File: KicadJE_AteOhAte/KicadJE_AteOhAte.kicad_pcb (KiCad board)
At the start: 2 copper layers, 100 x 100 mm, 201 parts, among them J201 In_Accent, J202 In Gate, J203 Out Tom, J301 PJRAS2X2S01AUX, J302 Conn_01x03, P201 Doepfer_Power_10pin, Q201 MMBT2222A, Q202 MMBT2222A, Q203 MMBT2222A, Q204 MMBT2222A, Q205 MMBT2907A, Q206 MMBT2222A, Q207 MMBT2222A, SW201 Con/Tom, U201 TL072, U202 TL072, U203 TL072, U301 TL072, U302 TL072, U303 TL072

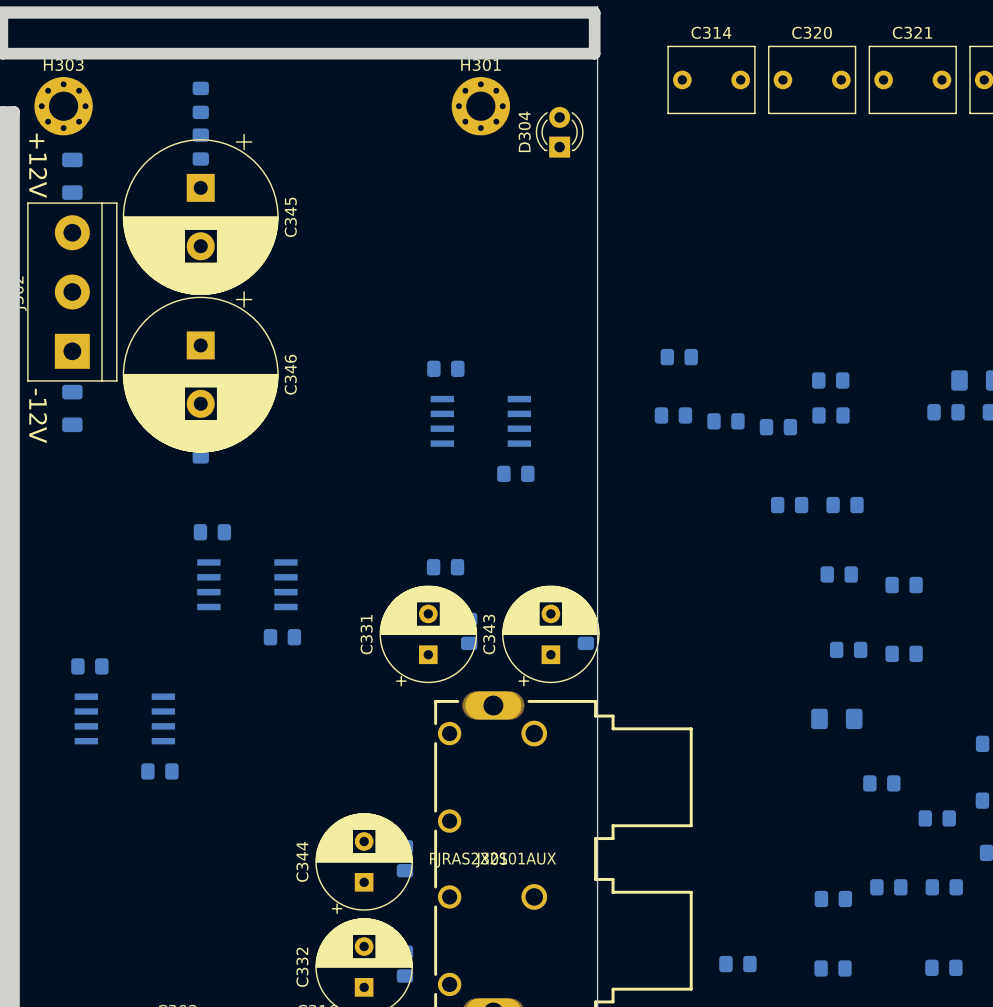
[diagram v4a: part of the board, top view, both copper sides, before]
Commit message: SCH Error in RIAA fixed (link C313 327 area)
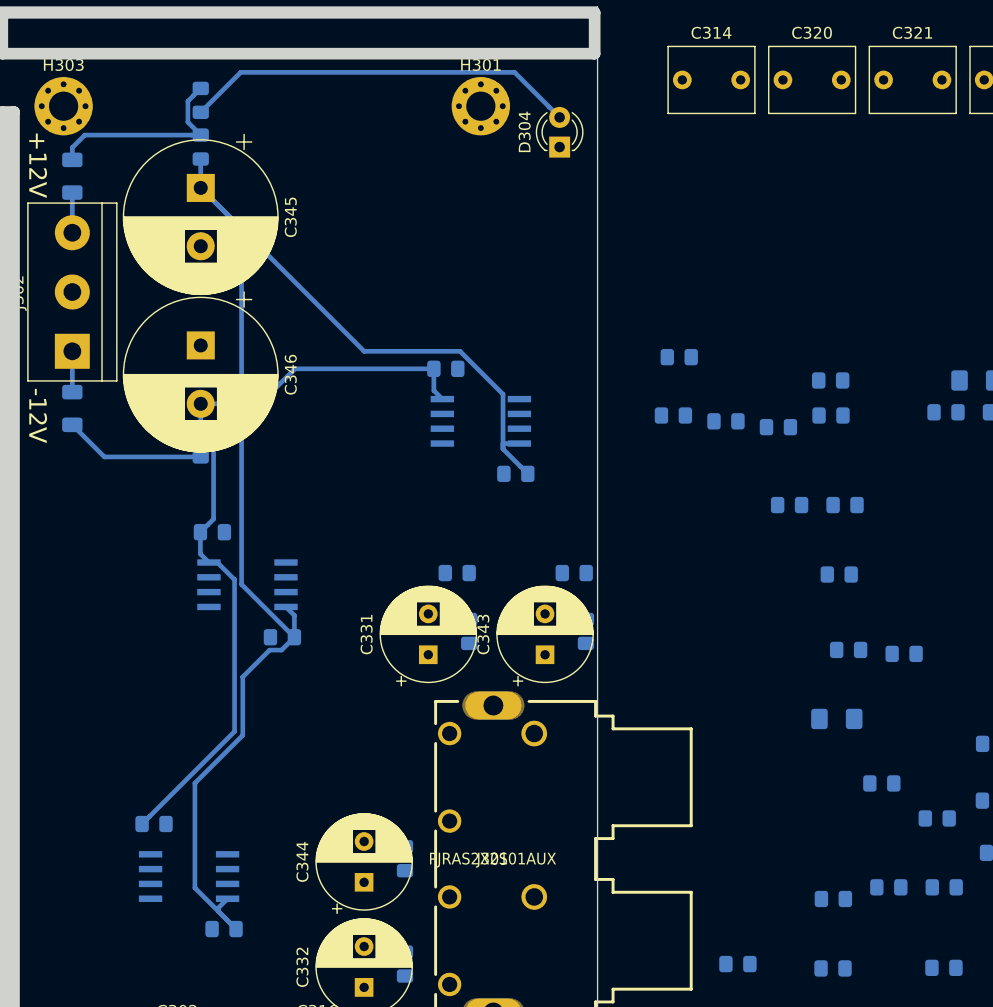
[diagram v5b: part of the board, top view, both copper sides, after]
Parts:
- moved R328 28.3 mm to (148.0, 98.5)
- moved C336 14.6 mm to (118.0, 129.0)
- moved C338 14.6 mm to (112.0, 120.0)
- moved U303 14.6 mm to (115.0, 124.5)
- moved R326 1.12 mm to (138.0, 98.5)
- moved C343 0.50 mm to (145.5, 105.5)
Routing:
- net +12V: track 238.2 -> 362.3 mm
- net -12V: track 154.8 -> 220.8 mm, vias 0 -> 2
- net Net-(D304-Pad2): track 0.00 -> 33.8 mm
- net Net-(F301-Pad2): track 0.00 -> 17.4 mm
- net Net-(D304-Pad1): track 0.00 -> 12.1 mm
- net /KicadJE_AteOhAte3/-PSU: track 0.00 -> 3.50 mm
- net /KicadJE_AteOhAte3/+PSU: track 0.00 -> 3.44 mm
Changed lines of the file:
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@@
     (thickness 1.6)
     (drawings 42)
-    (tracks 776)
+    (tracks 837)
     (zones 0)
     (modules 201)
@@
     (add_net /KicadJE_AteOhAte2/PinkNoise)
     (add_net /KicadJE_AteOhAte2/WhiteNoise)
-    (add_net /KicadJE_AteOhAte3/+PSU)
-    (add_net /KicadJE_AteOhAte3/-PSU)
     (add_net InAccent)
     (add_net InGate)
@@
     (add_net "Net-(D205-Pad1)")
     (add_net "Net-(D208-Pad2)")
-    (add_net "Net-(D304-Pad1)")
-    (add_net "Net-(D304-Pad2)")
-    (add_net "Net-(F301-Pad2)")
     (add_net "Net-(J201-PadT)")
     (add_net "Net-(J202-PadT)")
@@
     (add_net +12V)
     (add_net -12V)
+    (add_net /KicadJE_AteOhAte3/+PSU)
+    (add_net /KicadJE_AteOhAte3/-PSU)
     (add_net GND)
+    (add_net "Net-(D304-Pad1)")
+    (add_net "Net-(D304-Pad2)")
+    (add_net "Net-(F301-Pad2)")
   )
   (module AJ:Johansen_engineering_logo_25mm_front_neg5 (layer B.Cu)
@@
   )
   (module Capacitor_SMD:C_0805_2012Metric_Pad1.15x1.40mm_HandSolder (layer B.Cu)
-    (at 112.5 115.5)
+    (at 118 129)
     (descr "Capacitor SMD 0805 (2012 Metric), square (rectangular) end terminal, IPC_7351 nominal with elongated pad for handsoldering. (Body size source: https://docs.google.com/spreadsheets/d/1BsfQQcO9C6DZCsRaXUlFlo91Tg2WpOkGARC1WS5S8t0/edit?usp=sharing), generated with kicad-footprint-generator")
     (tags "capacitor handsolder")
@@
   )
   (module Capacitor_SMD:C_0805_2012Metric_Pad1.15x1.40mm_HandSolder (layer B.Cu)
-    (at 106.5 106.5)
+    (at 112 120)
     (descr "Capacitor SMD 0805 (2012 Metric), square (rectangular) end terminal, IPC_7351 nominal with elongated pad for handsoldering. (Body size source: https://docs.google.com/spreadsheets/d/1BsfQQcO9C6DZCsRaXUlFlo91Tg2WpOkGARC1WS5S8t0/edit?usp=sharing), generated with kicad-footprint-generator")
     (tags "capacitor handsolder")
@@
   )
   (module Resistor_SMD:R_0805_2012Metric_Pad1.15x1.40mm_HandSolder (layer B.Cu)
-    (at 136.975 98)
+    (at 137.975 98.5)
     (descr "Resistor SMD 0805 (2012 Metric), square (rectangular) end terminal, IPC_7351 nominal with elongated pad for handsoldering. (Body size source: https://docs.google.com/spreadsheets/d/1BsfQQcO9C6DZCsRaXUlFlo91Tg2WpOkGARC1WS5S8t0/edit?usp=sharing), generated with kicad-footprint-generator")
     (tags "resistor handsolder")
@@
   )
   (module Resistor_SMD:R_0805_2012Metric_Pad1.15x1.40mm_HandSolder (layer B.Cu)
-    (at 176.265001 99.524999)
+    (at 148 98.5)
     (descr "Resistor SMD 0805 (2012 Metric), square (rectangular) end terminal, IPC_7351 nominal with elongated pad for handsoldering. (Body size source: https://docs.google.com/spreadsheets/d/1BsfQQcO9C6DZCsRaXUlFlo91Tg2WpOkGARC1WS5S8t0/edit?usp=sharing), generated with kicad-footprint-generator")
     (tags "resistor handsolder")
@@
   )
   (module AJ-Dropbox-Kicad:AJ_SO-8_5.3x6.2mm_P1.27mm (layer B.Cu)
-    (at 109.5 111)
+    (at 115 124.5)
     (descr "8-Lead Plastic Small Outline, 5.3x6.2mm Body (http://www.ti.com.cn/cn/lit/ds/symlink/tl7705a.pdf)")
     (tags "SOIC 1.27")
@@
   )
   (module Capacitor_THT:CP_Radial_D8.0mm_P3.50mm (layer F.Cu)
-    (at 146 105.5 90)
+    (at 145.5 105.5 90)
     (descr "CP, Radial series, Radial, pin pitch=3.50mm, , diameter=8mm, Electrolytic Capacitor")
     (tags "CP Radial series Radial pin pitch 3.50mm  diameter 8mm Electrolytic Capacitor")
@@
   (segment (start 74.39996 122.60004) (end 72.475 124.525) (width 0.4) (layer B.Cu) (net 3))
   (segment (start 94 66) (end 91.46 66) (width 0.4) (layer F.Cu) (net 3) (status 30))
+  (segment (start 116 84) (end 116 86.5) (width 0.4) (layer B.Cu) (net 3))
+  (segment (start 116.598372 94.376628) (end 115.975 95) (width 0.4) (layer B.Cu) (net 3))
+  (segment (start 117.10001 93.87499) (end 116.598372 94.376628) (width 0.4) (layer B.Cu) (net 3))
+  (segment (start 117.10001 87.60001) (end 117.10001 93.87499) (width 0.4) (layer B.Cu) (net 3))
+  (segment (start 116 86.5) (end 117.10001 87.60001) (width 0.4) (layer B.Cu) (net 3))
+  (segment (start 115.975 96.87) (end 116.7 97.595) (width 0.4) (layer B.Cu) (net 3))
+  (segment (start 115.975 95) (end 115.975 96.87) (width 0.4) (layer B.Cu) (net 3))
+  (via (at 118.69999 84) (size 0.8) (drill 0.4) (layers F.Cu B.Cu) (net 3))
+  (segment (start 118.899989 112.075011) (end 111.598372 119.376628) (width 0.4) (layer B.Cu) (net 3))
+  (segment (start 111.598372 119.376628) (end 110.975 120) (width 0.4) (layer B.Cu) (net 3))
+  (segment (start 118.899989 99.069989) (end 118.899989 112.075011) (width 0.4) (layer B.Cu) (net 3))
+  (segment (start 117.425 97.595) (end 118.899989 99.069989) (width 0.4) (layer B.Cu) (net 3))
+  (segment (start 116.7 97.595) (end 117.425 97.595) (width 0.4) (layer B.Cu) (net 3))
+  (segment (start 116 84) (end 118.69999 84) (width 0.4) (layer B.Cu) (net 3))
+  (via (at 120.5 84) (size 0.8) (drill 0.4) (layers F.Cu B.Cu) (net 3))
+  (segment (start 118.69999 84) (end 120.5 84) (width 0.4) (layer F.Cu) (net 3))
+  (segment (start 121.065685 84) (end 120.5 84) (width 0.4) (layer B.Cu) (net 3))
+  (segment (start 135.975 81) (end 124.065685 81) (width 0.4) (layer B.Cu) (net 3))
+  (segment (start 124.065685 81) (end 121.065685 84) (width 0.4) (layer B.Cu) (net 3))
+  (segment (start 135.975 82.87) (end 136.7 83.595) (width 0.4) (layer B.Cu) (net 3))
+  (segment (start 135.975 81) (end 135.975 82.87) (width 0.4) (layer B.Cu) (net 3))
   (segment (start 81 126.8) (end 81 128.475) (width 0.4) (layer B.Cu) (net 4) (status 30))
   (segment (start 80.93 128.405) (end 81 128.475) (width 0.4) (layer B.Cu) (net 4) (status 30))
@@
   (segment (start 70.905 64.7) (end 70.905 67.905) (width 0.4) (layer B.Cu) (net 4) (status 10))
   (segment (start 70.905 67.905) (end 73 70) (width 0.4) (layer B.Cu) (net 4))
+  (segment (start 116 63.025) (end 116 65.5) (width 0.4) (layer B.Cu) (net 4))
+  (segment (start 124.025 102.13) (end 123.3 101.405) (width 0.4) (layer B.Cu) (net 4))
+  (segment (start 124.025 104) (end 124.025 102.13) (width 0.4) (layer B.Cu) (net 4))
+  (segment (start 143.401628 89.376628) (end 144.025 90) (width 0.4) (layer B.Cu) (net 4))
+  (segment (start 141.899999 87.874999) (end 143.401628 89.376628) (width 0.4) (layer B.Cu) (net 4))
+  (segment (start 141.899999 83.180743) (end 141.899999 87.874999) (width 0.4) (layer B.Cu) (net 4))
+  (segment (start 138.219256 79.5) (end 141.899999 83.180743) (width 0.4) (layer B.Cu) (net 4))
+  (segment (start 116 65.5) (end 130 79.5) (width 0.4) (layer B.Cu) (net 4))
+  (segment (start 130 79.5) (end 138.219256 79.5) (width 0.4) (layer B.Cu) (net 4))
+  (segment (start 117.5 127.205) (end 118.3 126.405) (width 0.4) (layer B.Cu) (net 4))
+  (segment (start 119.025 129) (end 117.5 127.475) (width 0.4) (layer B.Cu) (net 4))
+  (segment (start 117.5 127.475) (end 117.5 127.205) (width 0.4) (layer B.Cu) (net 4))
+  (segment (start 115.5 125.475) (end 119.025 129) (width 0.4) (layer B.Cu) (net 4))
+  (segment (start 122.92499 105.10001) (end 121.89999 105.10001) (width 0.4) (layer B.Cu) (net 4))
+  (segment (start 124.025 104) (end 122.92499 105.10001) (width 0.4) (layer B.Cu) (net 4))
+  (segment (start 121.89999 105.10001) (end 119.60001 107.39999) (width 0.4) (layer B.Cu) (net 4))
+  (segment (start 119.60001 107.39999) (end 119.60001 112.39999) (width 0.4) (layer B.Cu) (net 4))
+  (segment (start 119.60001 112.39999) (end 115.5 116.5) (width 0.4) (layer B.Cu) (net 4))
+  (segment (start 115.5 116.5) (end 115.5 125.475) (width 0.4) (layer B.Cu) (net 4))
+  (segment (start 116 65.5) (end 119.5 69) (width 0.4) (layer B.Cu) (net 4))
+  (segment (start 119.5 69) (end 119.5 99.475) (width 0.4) (layer B.Cu) (net 4))
+  (segment (start 119.5 99.475) (end 124.025 104) (width 0.4) (layer B.Cu) (net 4))
+  (segment (start 141.9 87.405) (end 143.3 87.405) (width 0.4) (layer B.Cu) (net 4))
+  (segment (start 141.899999 87.874999) (end 141.9 87.405) (width 0.4) (layer B.Cu) (net 4))
   (segment (start 65.549999 142.7) (end 65.575 142.674999) (width 0.15) (layer B.Cu) (net 9) (status 30))
   (segment (start 63.875 142.7) (end 65.549999 142.7) (width 0.15) (layer B.Cu) (net 9) (status 30))
@@
   (segment (start 73.774989 126.5) (end 72.485 126.5) (width 0.15) (layer B.Cu) (net 65))
   (segment (start 72.485 126.5) (end 71.85 127.135) (width 0.15) (layer B.Cu) (net 65))
+  (segment (start 145.850001 58.560001) (end 146.75 59.46) (width 0.4) (layer B.Cu) (net 90))
+  (segment (start 142.889999 55.599999) (end 145.850001 58.560001) (width 0.4) (layer B.Cu) (net 90))
+  (segment (start 119.425001 55.599999) (end 142.889999 55.599999) (width 0.4) (layer B.Cu) (net 90))
+  (segment (start 116 59.025) (end 119.425001 55.599999) (width 0.4) (layer B.Cu) (net 90))
+  (segment (start 107.75 88.55) (end 105 85.8) (width 0.4) (layer B.Cu) (net 91))
+  (segment (start 116 88.55) (end 107.75 88.55) (width 0.4) (layer B.Cu) (net 91))
+  (segment (start 105 79.5) (end 105 83) (width 0.4) (layer B.Cu) (net 100))
+  (segment (start 105 69.34) (end 105 65.9) (width 0.4) (layer B.Cu) (net 101))
+  (segment (start 115.2 60.975) (end 116 60.975) (width 0.4) (layer B.Cu) (net 102))
+  (segment (start 106.067002 60.975) (end 115.2 60.975) (width 0.4) (layer B.Cu) (net 102))
+  (segment (start 105 62.042002) (end 106.067002 60.975) (width 0.4) (layer B.Cu) (net 102))
+  (segment (start 105 63.1) (end 105 62.042002) (width 0.4) (layer B.Cu) (net 102))
+  (segment (start 115.376628 57.598372) (end 116 56.975) (width 0.4) (layer B.Cu) (net 102))
+  (segment (start 114.89999 58.07501) (end 115.376628 57.598372) (width 0.4) (layer B.Cu) (net 102))
+  (segment (start 114.89999 59.87499) (end 114.89999 58.07501) (width 0.4) (layer B.Cu) (net 102))
+  (segment (start 116 60.975) (end 114.89999 59.87499) (width 0.4) (layer B.Cu) (net 102))
   (zone (net 1) (net_name GND) (layer B.Cu) (hatch edge 0.508)
     (connect_pads (clearance 0.508))

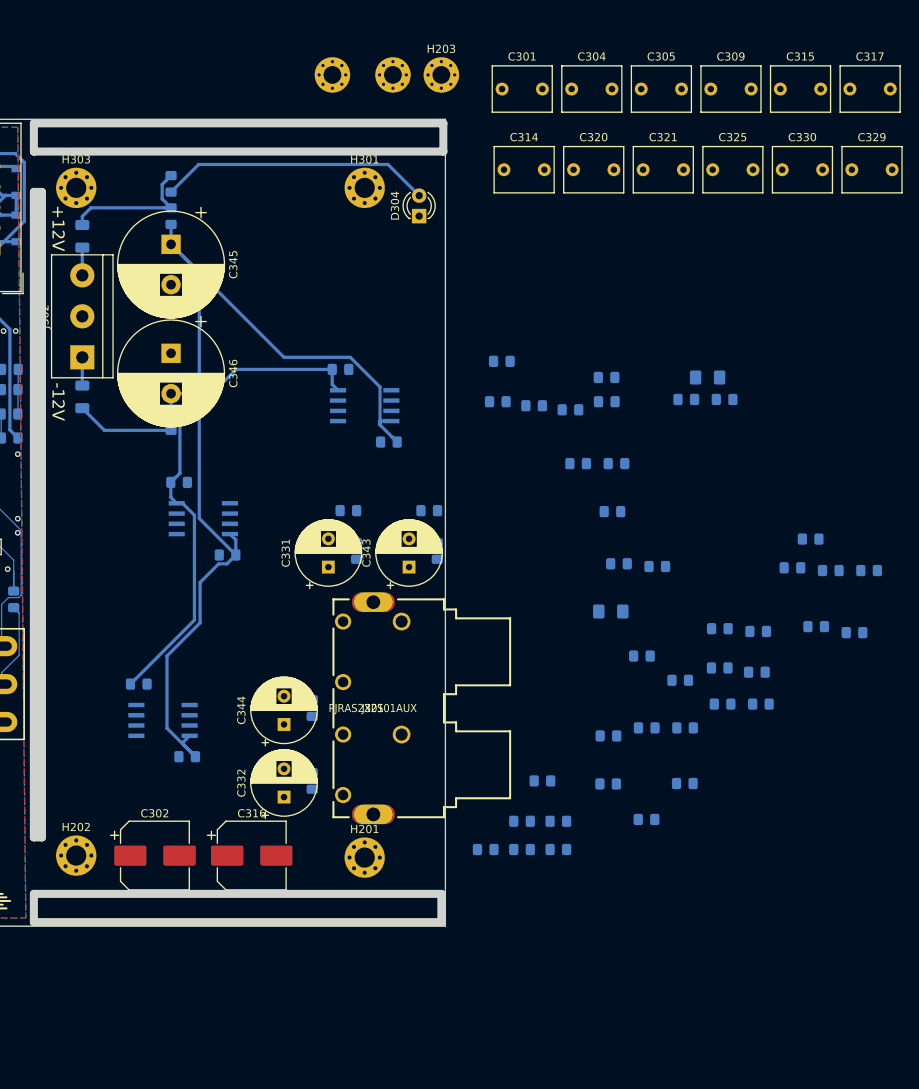
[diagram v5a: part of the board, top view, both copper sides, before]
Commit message: 90% component placement RIAA
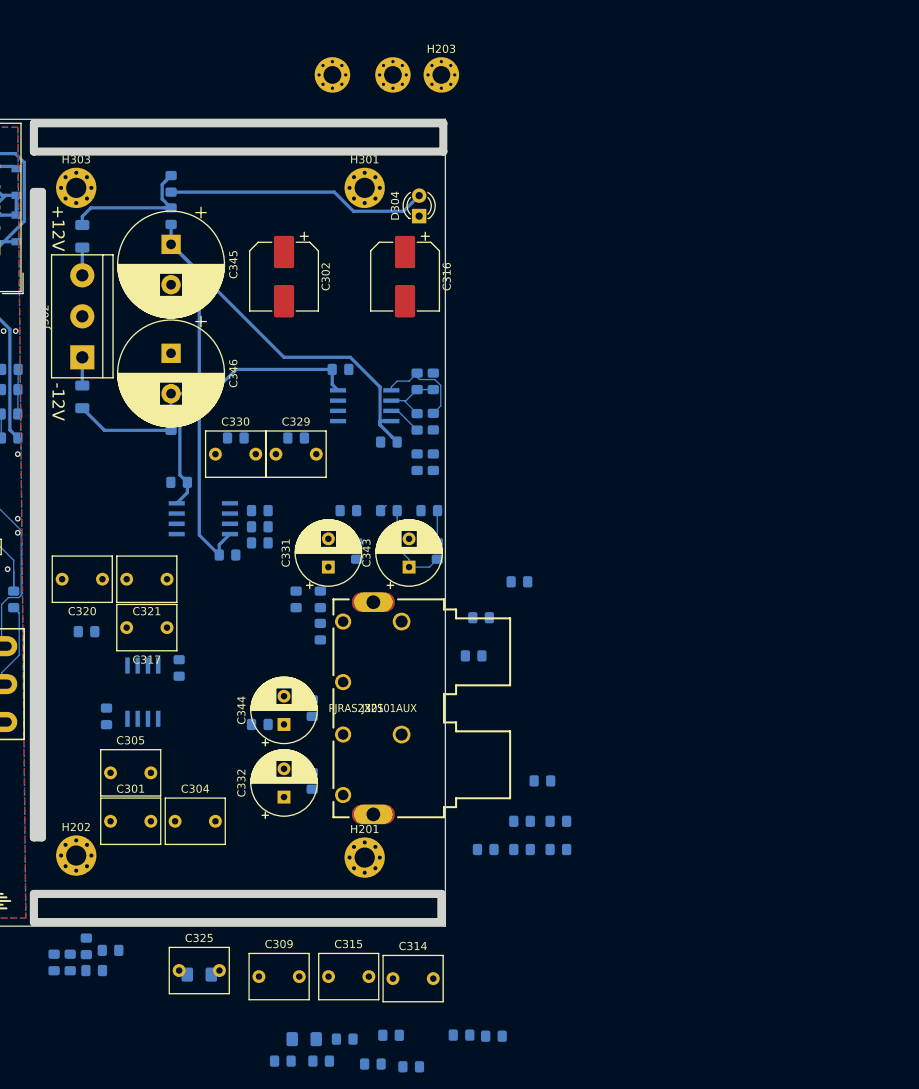
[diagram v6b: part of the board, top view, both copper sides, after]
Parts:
- moved C309 123.4 mm to (126.9, 156.2)
- moved C315 123.4 mm to (135.5, 156.2)
- moved C325 119.3 mm to (117.0, 155.5)
- moved C317 107.8 mm to (115.5, 113.0), turned to 180 degrees
- moved C305 107.3 mm to (108.5, 131.0)
- moved C304 103.2 mm to (116.5, 137.0)
- moved C301 102.9 mm to (108.5, 137.0)
- moved C314 101.2 mm to (143.5, 156.5)
- moved R323 99.1 mm to (106.5, 155.5), turned to 180 degrees
- moved C311 96.0 mm to (132.5, 164.0)
- moved R308 96.0 mm to (129.9, 166.7)
- moved R312 96.0 mm to (134.6, 166.7)
- moved R316 95.2 mm to (105.5, 113.5)
- moved C319 94.2 mm to (101.5, 154.5), turned to 90 degrees
- moved C324 87.4 mm to (103.5, 154.5), turned to 90 degrees
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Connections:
- C314 pad 1: Net-(C314-Pad1) -> Net-(C312-Pad1)
- C315 pad 2: Net-(C314-Pad1) -> Net-(C312-Pad1)
- C329 pad 1: Net-(C329-Pad1) -> Net-(C327-Pad1)
- C330 pad 2: Net-(C329-Pad1) -> Net-(C327-Pad1)
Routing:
- net +12V: track 362.3 -> 327.5 mm
- net -12V: track 220.8 -> 193.9 mm
- net Net-(C318-Pad2): track 0.00 -> 12.3 mm
- net In_R: track 0.00 -> 11.5 mm
- net Net-(C318-Pad1): track 0.00 -> 8.54 mm
- net R_GainOut: track 0.00 -> 4.19 mm
- net Net-(C341-Pad1): track 0.00 -> 3.99 mm
- net Net-(D304-Pad2): track 33.8 -> 32.5 mm
- net Net-(C322-Pad1): track 0.00 -> 0.95 mm

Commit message: RIAA Placed and initial route
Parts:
- moved C312 79.5 mm to (125.5, 88.5)
- moved R312 77.6 mm to (112.0, 92.5)
- moved R302 77.4 mm to (134.0, 89.5), turned to 90 degrees
- moved C313 75.7 mm to (125.5, 94.5)
- moved R313 75.3 mm to (112.0, 95.0)
- moved R304 73.1 mm to (112.0, 100.0), turned to 180 degrees
- moved C314 72.9 mm to (123.0, 86.5)
- moved R305 71.2 mm to (112.0, 97.5)
- moved C311 67.6 mm to (105.5, 102.0)
- moved R308 66.4 mm to (105.5, 105.0), turned to 180 degrees
- moved R303 65.3 mm to (105.5, 111.5), turned to 180 degrees
- moved C307 65.1 mm to (105.5, 108.5), turned to 180 degrees
- moved C315 65.0 mm to (123.0, 92.5)
- moved C309 60.9 mm to (102.9, 100.2)
- moved R309 59.3 mm to (105.5, 114.0), turned to 180 degrees
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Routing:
- net Net-(D304-Pad1): track 12.1 -> 86.5 mm
- net Net-(C310-Pad1): track 0.00 -> 62.1 mm, vias 0 -> 2
- net Out_L: track 0.00 -> 56.0 mm
- net Net-(C317-Pad1): track 0.00 -> 37.8 mm
- net Net-(C304-Pad2): track 0.00 -> 32.6 mm
- net +12V: track 327.5 -> 359.4 mm
- net Net-(C322-Pad1): track 0.95 -> 30.5 mm
- net -12V: track 193.9 -> 223.1 mm
- net Net-(C306-Pad1): track 0.00 -> 25.4 mm, vias 0 -> 2
- net Net-(C312-Pad1): track 0.00 -> 23.6 mm, vias 0 -> 2
- net Net-(C301-Pad1): track 0.00 -> 23.2 mm
- net Net-(C313-Pad1): track 0.00 -> 19.3 mm, vias 0 -> 2
- net Net-(C327-Pad1): track 0.00 -> 19.2 mm
- net R_Rumble_Out: track 0.00 -> 17.9 mm
- net Net-(C316-Pad1): track 0.00 -> 17.6 mm, vias 0 -> 1
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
